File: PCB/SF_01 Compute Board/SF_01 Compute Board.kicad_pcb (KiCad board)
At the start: 4 copper layers, 128 x 128 mm, 326 parts, among them J1 SS-53200-001, J10 SUBWOOFER_6, J11 TWEETER_1, J12 TWEETER_2, J13 TWEETER_3, J14 TWEETER_4, J15 USB_C_Receptacle_USB2.0_16P, J16 USB_C_Receptacle_USB2.0_16P, J2 Barrel_Jack, J3 UART, J4 JTAG, J5 SUBWOOFER_1, J6 SUBWOOFER_2, J7 SUBWOOFER_3, J8 SUBWOOFER_4, J9 SUBWOOFER_5, SW1 POWER, SW2 PI_BOOT, SW3 ESP_BOOT, SW4 ESP_RESET, U1 CM4102008, U10 TPD4E02B04DQA, U11 LP5907MFX-3.3, U12 TS5A3159AYZPR, U13 TS5A3159AYZPR, U14 PCM5102A, U15 TS5A3159AYZPR, U16 TS5A3159AYZPR, U17 TPA3116D2DAD, U18 TPA3116D2DAD, U19 TPA3116D2DAD, U2 TPD4E02B04DQA, U20 TPA3130D2DAPR, U21 TPA3130D2DAPR, U22 MPU-6050, U23 BME680, U24 TS5A3159AYZPR, U25 TS5A3159AYZPR, U26 TS5A3159AYZPR, U3 TPD4E02B04DQA, U4 ESP32-S3-WROOM-2, U5 PCM5102A, U6 RT9742SNGV, U7 TPD4E02B04DQA, U8 74LVC1G07, U9 74LVC1G07

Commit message: Added USB Host control, Routed 1st amplifier
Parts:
- added C45: 100nF, Capacitor_SMD:C_0603_1608Metric, F.Cu at (168.2, 131.4)
- added C47: 100nF, Capacitor_SMD:C_0603_1608Metric, F.Cu at (165.0, 127.0)
- added C73: 22uF, Capacitor_SMD:CP_Elec_4x3, F.Cu at (161.7, 128.7)
- added R12: 10K, Resistor_SMD:R_0603_1608Metric, F.Cu at (168.2, 129.8)
- added SW6: SW_DPDT_x2, Button_Switch_THT:SW_Push_2P2T_Toggle_CK_PVA2xxH1xxxxxxV2, F.Cu at (162.8, 117.4)
- added U27: TPS2041B, Package_TO_SOT_SMD:SOT-23-5, F.Cu at (168.2, 127.3)
- L13, L14, L15, L16, L17, L18, L19, L20: value 10uH/10A -> 10uH/3A; footprint Inductor_SMD:L_10.4x10.4_H4.8 -> Inductor_SMD:L_APV_ANR4020
- moved R25 447.0 mm to (-8.46, 70.9)
- moved R26 447.0 mm to (-8.46, 73.4)
- moved R27 447.0 mm to (-8.46, 75.9)
- moved R28 447.0 mm to (-8.46, 78.4)
- moved R29 447.0 mm to (-8.46, 81.0)
- moved R30 447.0 mm to (-8.46, 83.5)
- moved C127 394.0 mm to (53.6, 98.3)
- moved C75 394.0 mm to (41.6, 83.3)
- moved C76 394.0 mm to (41.6, 85.8)
- moved C77 394.0 mm to (41.6, 88.3)
- moved C79 394.0 mm to (41.6, 90.8)
- moved C80 394.0 mm to (41.6, 93.3)
- moved C81 394.0 mm to (41.6, 95.8)
- moved C82 394.0 mm to (41.6, 98.3)
- moved C84 394.0 mm to (41.6, 100.9)
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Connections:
- C115 pad 2: Net-(J9-Pin_1) -> Net-(J9-Pin_2)
- C116 pad 1: Net-(J9-Pin_2) -> Net-(J9-Pin_1)
- C117 pad 2: Net-(J10-Pin_1) -> Net-(J10-Pin_2)
- C118 pad 1: Net-(J10-Pin_2) -> Net-(J10-Pin_1)
- C119 pad 2: Net-(J9-Pin_1) -> Net-(J9-Pin_2)
- C120 pad 1: Net-(J9-Pin_2) -> Net-(J9-Pin_1)
- C121 pad 2: Net-(J10-Pin_1) -> Net-(J10-Pin_2)
- C122 pad 1: Net-(J10-Pin_2) -> Net-(J10-Pin_1)
- C145 pad 2: Net-(J11-Pin_1) -> Net-(J11-Pin_2)
- C146 pad 1: Net-(J11-Pin_2) -> Net-(J11-Pin_1)
- C147 pad 2: Net-(J12-Pin_1) -> Net-(J12-Pin_2)
- C148 pad 1: Net-(J12-Pin_2) -> Net-(J12-Pin_1)
- C149 pad 2: Net-(J11-Pin_1) -> Net-(J11-Pin_2)
- C150 pad 1: Net-(J11-Pin_2) -> Net-(J11-Pin_1)
- C151 pad 2: Net-(J12-Pin_1) -> Net-(J12-Pin_2)
- C152 pad 1: Net-(J12-Pin_2) -> Net-(J12-Pin_1)
- C173 pad 2: Net-(J13-Pin_1) -> Net-(J13-Pin_2)
- C174 pad 1: Net-(J13-Pin_2) -> Net-(J13-Pin_1)
- C175 pad 2: Net-(J14-Pin_1) -> Net-(J14-Pin_2)
- C176 pad 1: Net-(J14-Pin_2) -> Net-(J14-Pin_1)
- C177 pad 2: Net-(J13-Pin_1) -> Net-(J13-Pin_2)
- C178 pad 1: Net-(J13-Pin_2) -> Net-(J13-Pin_1)
- C179 pad 2: Net-(J14-Pin_1) -> Net-(J14-Pin_2)
- C180 pad 1: Net-(J14-Pin_2) -> Net-(J14-Pin_1)
- C40 pad 1: VSYS -> SYS_5V
- C41 pad 1: SYS_5V -> VSYS
- C59 pad 2: Net-(J5-Pin_1) -> Net-(J5-Pin_2)
- C60 pad 1: Net-(J5-Pin_2) -> Net-(J5-Pin_1)
- C61 pad 2: Net-(J5-Pin_1) -> Net-(J5-Pin_2)
- C62 pad 1: Net-(J5-Pin_2) -> Net-(J5-Pin_1)
- C65 pad 2: Net-(J6-Pin_1) -> Net-(J6-Pin_2)
- C66 pad 1: Net-(J6-Pin_2) -> Net-(J6-Pin_1)
- C67 pad 2: Net-(J6-Pin_1) -> Net-(J6-Pin_2)
- C68 pad 1: Net-(J6-Pin_2) -> Net-(J6-Pin_1)
- C88 pad 2: Net-(J7-Pin_1) -> Net-(J7-Pin_2)
- C89 pad 1: Net-(J7-Pin_2) -> Net-(J7-Pin_1)
- C90 pad 2: Net-(J8-Pin_1) -> Net-(J8-Pin_2)
- C91 pad 1: Net-(J8-Pin_2) -> Net-(J8-Pin_1)
- C92 pad 2: Net-(J7-Pin_1) -> Net-(J7-Pin_2)
- C93 pad 1: Net-(J7-Pin_2) -> Net-(J7-Pin_1)
- C94 pad 2: Net-(J8-Pin_1) -> Net-(J8-Pin_2)
- C95 pad 1: Net-(J8-Pin_2) -> Net-(J8-Pin_1)
- J15 pad A4: SYS_5V -> VBUS
- J15 pad A9: SYS_5V -> VBUS
- J15 pad B4: SYS_5V -> VBUS
- J15 pad B9: SYS_5V -> VBUS
- J16 pad A4: SYS_5V -> Net-(J16-VBUS-PadA4)
- J16 pad A9: SYS_5V -> Net-(J16-VBUS-PadA4)
- J16 pad B4: SYS_5V -> Net-(J16-VBUS-PadA4)
- J16 pad B9: SYS_5V -> Net-(J16-VBUS-PadA4)
- L1 pad 2: Net-(J5-Pin_1) -> Net-(J5-Pin_2)
- L10 pad 2: Net-(J9-Pin_2) -> Net-(J9-Pin_1)
- L11 pad 2: Net-(J10-Pin_1) -> Net-(J10-Pin_2)
- L12 pad 2: Net-(J10-Pin_2) -> Net-(J10-Pin_1)
- L13 pad 2: Net-(J11-Pin_1) -> Net-(J11-Pin_2)
- L14 pad 2: Net-(J11-Pin_2) -> Net-(J11-Pin_1)
- L15 pad 2: Net-(J12-Pin_1) -> Net-(J12-Pin_2)
- L16 pad 2: Net-(J12-Pin_2) -> Net-(J12-Pin_1)
- L17 pad 2: Net-(J13-Pin_1) -> Net-(J13-Pin_2)
- L18 pad 2: Net-(J13-Pin_2) -> Net-(J13-Pin_1)
- L19 pad 2: Net-(J14-Pin_1) -> Net-(J14-Pin_2)
- L2 pad 2: Net-(J5-Pin_2) -> Net-(J5-Pin_1)
- L20 pad 2: Net-(J14-Pin_2) -> Net-(J14-Pin_1)
- L3 pad 2: Net-(J6-Pin_1) -> Net-(J6-Pin_2)
- L4 pad 2: Net-(J6-Pin_2) -> Net-(J6-Pin_1)
- L5 pad 2: Net-(J7-Pin_1) -> Net-(J7-Pin_2)
- L6 pad 2: Net-(J7-Pin_2) -> Net-(J7-Pin_1)
- L7 pad 2: Net-(J8-Pin_1) -> Net-(J8-Pin_2)
- L8 pad 2: Net-(J8-Pin_2) -> Net-(J8-Pin_1)
- L9 pad 2: Net-(J9-Pin_1) -> Net-(J9-Pin_2)
- R21 pad 1: Net-(J5-Pin_1) -> Net-(J5-Pin_2)
- R22 pad 2: Net-(J5-Pin_2) -> Net-(J5-Pin_1)
- R23 pad 1: Net-(J6-Pin_1) -> Net-(J6-Pin_2)
- R24 pad 2: Net-(J6-Pin_2) -> Net-(J6-Pin_1)
- R31 pad 1: Net-(J7-Pin_1) -> Net-(J7-Pin_2)
- R32 pad 2: Net-(J7-Pin_2) -> Net-(J7-Pin_1)
- R33 pad 1: Net-(J8-Pin_1) -> Net-(J8-Pin_2)
- R34 pad 2: Net-(J8-Pin_2) -> Net-(J8-Pin_1)
- R40 pad 1: Net-(J9-Pin_1) -> Net-(J9-Pin_2)
- R41 pad 2: Net-(J9-Pin_2) -> Net-(J9-Pin_1)
- R42 pad 1: Net-(J10-Pin_1) -> Net-(J10-Pin_2)
- R43 pad 2: Net-(J10-Pin_2) -> Net-(J10-Pin_1)
- R51 pad 1: Net-(J11-Pin_1) -> Net-(J11-Pin_2)
- R52 pad 2: Net-(J11-Pin_2) -> Net-(J11-Pin_1)
- R53 pad 1: Net-(J12-Pin_1) -> Net-(J12-Pin_2)
- R54 pad 2: Net-(J12-Pin_2) -> Net-(J12-Pin_1)
- R61 pad 1: Net-(J13-Pin_1) -> Net-(J13-Pin_2)
- R62 pad 2: Net-(J13-Pin_2) -> Net-(J13-Pin_1)
- R63 pad 1: Net-(J14-Pin_1) -> Net-(J14-Pin_2)
- R64 pad 2: Net-(J14-Pin_2) -> Net-(J14-Pin_1)
- U1 pad 101: unconnected-(U1B-USB_OTG_ID-Pad101) -> Net-(SW6A-B)
- VR1 pad 2: VSYS -> SYS_5V
- VR1 pad 3: SYS_5V -> VSYS
- VR1 pad 4: VSYS -> SYS_5V
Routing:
- net GND: track 415.0 -> 556.7 mm, vias 320 -> 475
- net VBUS: track 0.00 -> 107.6 mm, vias 0 -> 3
- net Net-(U14-DIN): track 0.00 -> 79.0 mm, vias 0 -> 2
- net Net-(U14-BCK): track 0.00 -> 78.4 mm, vias 0 -> 2
- net Net-(U14-SCK): track 0.00 -> 77.5 mm, vias 0 -> 2
- net Net-(U14-LRCK): track 0.00 -> 76.4 mm, vias 0 -> 2
- net WOOFER_1: track 7.51 -> 71.3 mm, vias 0 -> 2
- net VSYS: track 72.2 -> 133.0 mm, vias 95 -> 134
- net WOOFER_2: track 2.34 -> 60.0 mm, vias 0 -> 2
- net SYS_5V: track 43.5 -> 77.5 mm
- net Net-(U17-GVDD): track 0.00 -> 29.9 mm, vias 0 -> 2
- net WOOFER_MUTE: track 0.00 -> 29.1 mm, vias 0 -> 2
- net Net-(U14-XSMT): track 78.5 -> 107.4 mm, vias 2 -> 4
- net Net-(U17-GAIN/SLV): track 0.00 -> 27.8 mm, vias 0 -> 2
- net Net-(SW6A-B): track 0.00 -> 27.4 mm, vias 0 -> 2
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
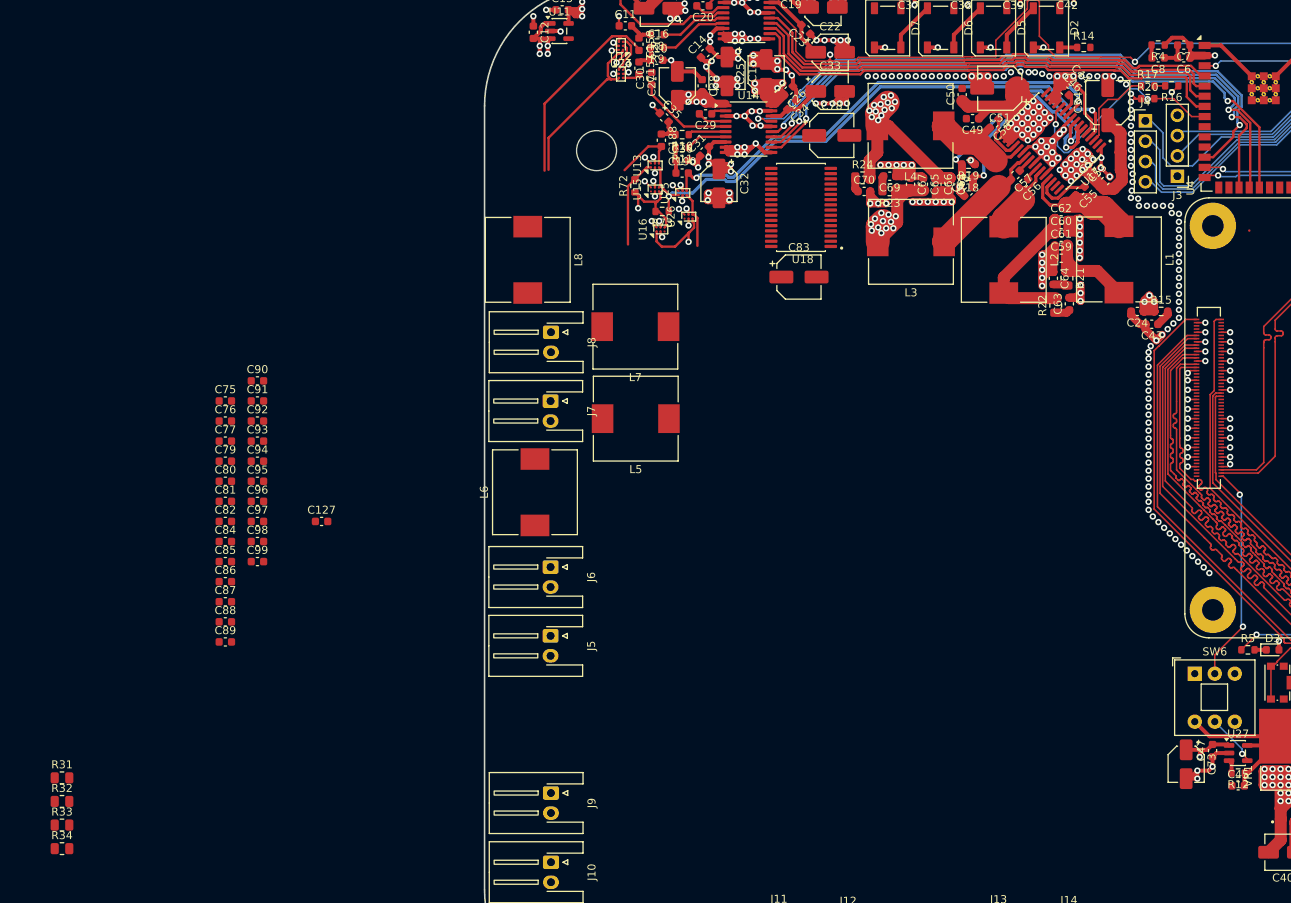
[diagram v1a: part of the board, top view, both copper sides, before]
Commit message: Routed 2nd Subwoofer Amplifier
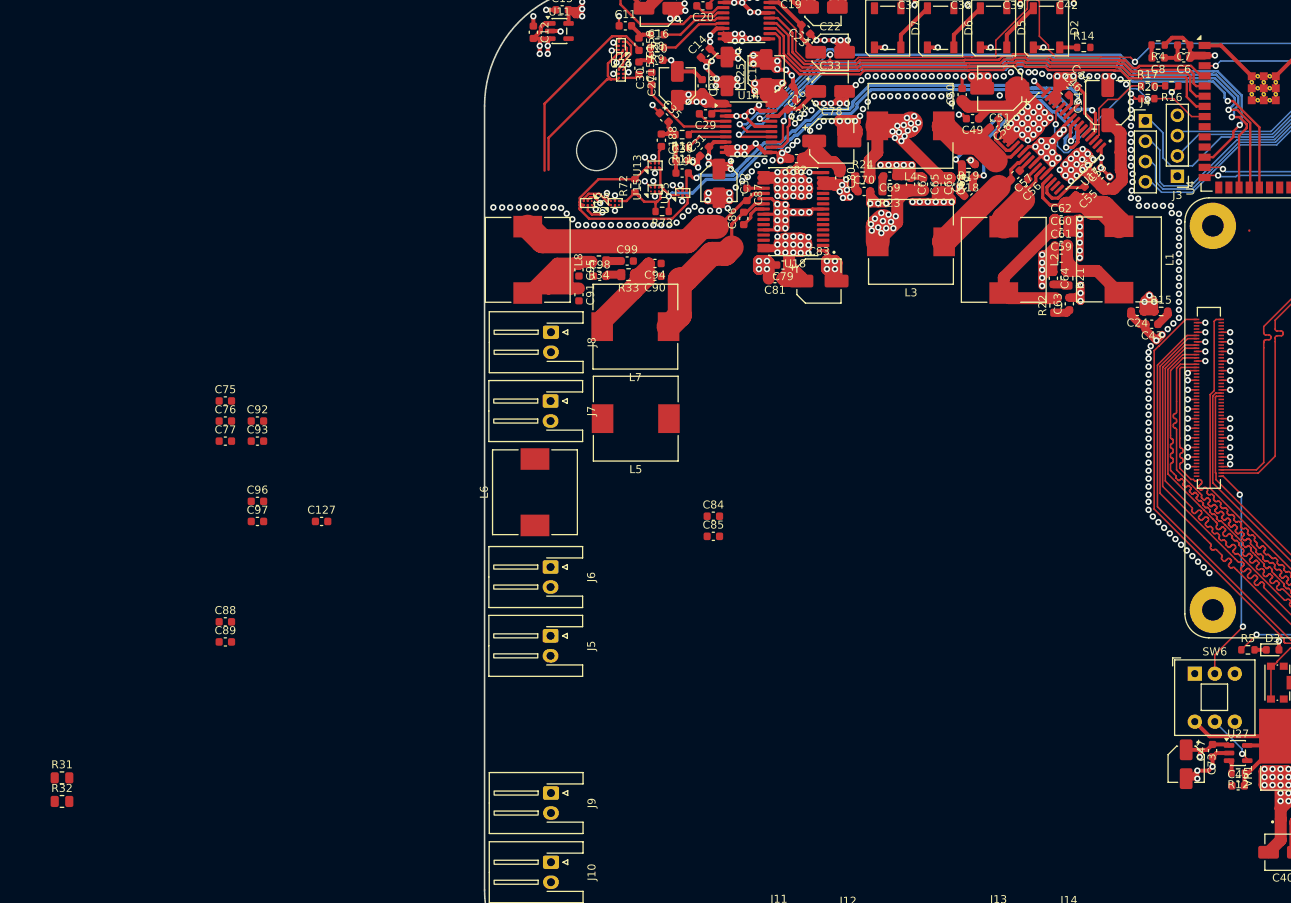
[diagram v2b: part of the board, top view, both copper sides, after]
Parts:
- moved R34 99.4 mm to (88.3, 65.9), turned to 180 degrees
- moved R33 98.7 mm to (92.0, 67.5), turned to 180 degrees
- moved C80 85.7 mm to (118.4, 55.4), turned to -90 degrees
- moved C82 84.6 mm to (113.0, 53.0), turned to 180 degrees
- moved C87 82.7 mm to (106.8, 57.5), turned to -90 degrees
- moved C86 79.1 mm to (106.4, 60.5), turned to 90 degrees
- moved C81 74.1 mm to (110.3, 68.0), turned to 180 degrees
- moved C79 73.9 mm to (111.3, 66.3), turned to 180 degrees
- moved C84 61.1 mm to (102.6, 97.7)
- moved C85 61.1 mm to (102.6, 100.2)
- moved C99 59.6 mm to (91.8, 65.8)
- moved C94 55.5 mm to (95.3, 66.1), turned to 180 degrees
- moved C98 54.1 mm to (88.4, 67.7)
- moved C90 51.4 mm to (95.3, 67.7), turned to 180 degrees
- moved C95 48.1 mm to (85.8, 66.9), turned to -90 degrees
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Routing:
- net GND: track 556.7 -> 620.7 mm, vias 475 -> 570
- net VSYS: track 133.0 -> 168.3 mm, vias 134 -> 167
- net Net-(U18-OUTNL): track 0.00 -> 32.7 mm
- net Net-(J8-Pin_1): track 0.00 -> 24.0 mm
- net Net-(J8-Pin_2): track 0.00 -> 23.6 mm
- net Net-(U18-OUTPL): track 0.00 -> 22.6 mm
- net WOOFER_6: track 18.1 -> 29.6 mm
- net Net-(U14-LRCK): track 76.4 -> 83.6 mm
- net Net-(U14-DIN): track 79.0 -> 86.0 mm
- net WOOFER_5: track 8.20 -> 2.37 mm
- net WOOFER_4: track 9.62 -> 4.62 mm, vias 1 -> 0
- net Net-(U18-BSPL): track 0.00 -> 3.55 mm
- net 3V3_A: track 69.4 -> 71.8 mm
- net Net-(U18-BSNL): track 0.00 -> 2.08 mm
- net AMP_CLK_SYNC: track 0.00 -> 2.07 mm, vias 0 -> 1
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
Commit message: Finished Routing 2nd Amplifier, started routing 3rd
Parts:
- moved C123 430.8 mm to (40.8, 136.5)
- moved C124 430.8 mm to (40.8, 139.0)
- moved C102 420.8 mm to (23.0, 125.2)
- moved C103 420.8 mm to (23.0, 127.7)
- moved C105 420.8 mm to (27.0, 95.1)
- moved C111 420.8 mm to (27.0, 107.7)
- moved C112 420.8 mm to (27.0, 110.2)
- moved C113 420.8 mm to (27.0, 112.7)
- moved C114 420.8 mm to (27.0, 115.2)
- moved C115 420.8 mm to (27.0, 117.7)
- moved C116 420.8 mm to (27.0, 120.2)
- moved C119 420.8 mm to (27.0, 127.7)
- moved C120 420.8 mm to (31.0, 95.1)
- moved C128 418.7 mm to (36.0, 119.5)
- moved R35 418.7 mm to (40.0, 117.0)
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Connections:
- C65 pad 2: Net-(J6-Pin_2) -> Net-(J6-Pin_1)
- C66 pad 1: Net-(J6-Pin_1) -> Net-(J6-Pin_2)
- C67 pad 2: Net-(J6-Pin_2) -> Net-(J6-Pin_1)
- C68 pad 1: Net-(J6-Pin_1) -> Net-(J6-Pin_2)
- L3 pad 2: Net-(J6-Pin_2) -> Net-(J6-Pin_1)
- L4 pad 2: Net-(J6-Pin_1) -> Net-(J6-Pin_2)
- R23 pad 1: Net-(J6-Pin_2) -> Net-(J6-Pin_1)
- R24 pad 2: Net-(J6-Pin_1) -> Net-(J6-Pin_2)
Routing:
- net Net-(J5-Pin_2): track 13.0 -> 196.3 mm, vias 0 -> 16
- net Net-(J6-Pin_2): track 15.9 -> 192.3 mm, vias 12 -> 16
- net Net-(J5-Pin_1): track 21.9 -> 169.9 mm, vias 0 -> 16
- net Net-(J6-Pin_1): track 25.0 -> 139.8 mm, vias 13 -> 16
- net GND: track 620.7 -> 704.7 mm, vias 570 -> 590
- net AMP_CLK_SYNC: track 2.07 -> 41.9 mm, vias 1 -> 2
- net Net-(J7-Pin_1): track 0.00 -> 36.5 mm
- net Net-(U18-OUTPR): track 0.00 -> 35.0 mm
- net WOOFER_4: track 4.62 -> 35.9 mm, vias 0 -> 2
- net Net-(J10-Pin_2): track 0.00 -> 29.4 mm
- net Net-(U18-GVDD): track 0.00 -> 29.0 mm, vias 0 -> 2
- net Net-(U18-FAULTZ): track 0.00 -> 26.8 mm, vias 0 -> 2
- net Net-(J10-Pin_1): track 0.00 -> 25.1 mm
- net WOOFER_3: track 8.55 -> 33.5 mm, vias 0 -> 2
- net Net-(U18-GAIN/SLV): track 0.00 -> 24.2 mm, vias 0 -> 2
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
